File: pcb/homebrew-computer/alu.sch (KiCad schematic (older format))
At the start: 8 parts

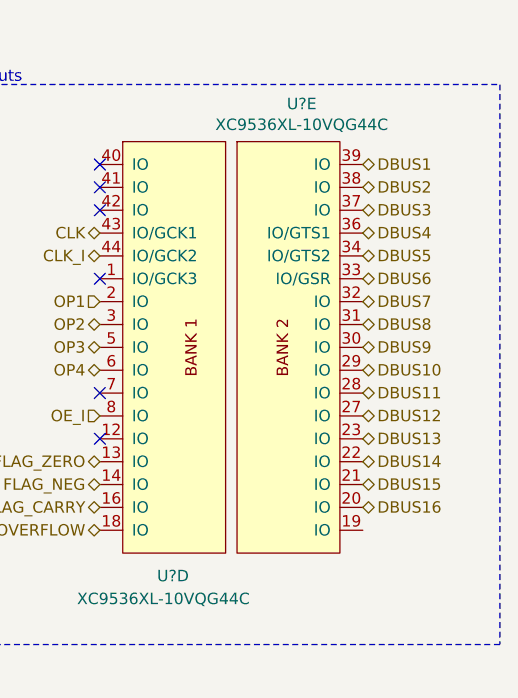
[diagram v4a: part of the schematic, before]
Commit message: Remove the address bus as it would require too big of a connector
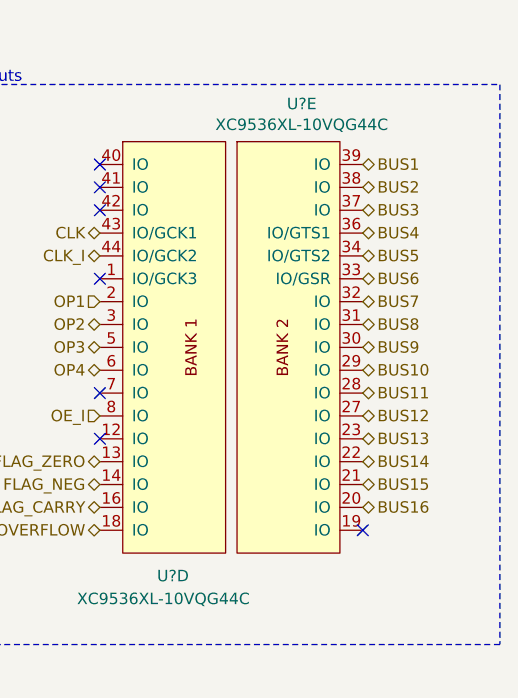
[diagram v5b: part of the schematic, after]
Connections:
- net DBUS1 renamed BUS1
- net DBUS10 renamed BUS10
- net DBUS11 renamed BUS11
- net DBUS12 renamed BUS12
- net DBUS13 renamed BUS13
- net DBUS14 renamed BUS14
- net DBUS15 renamed BUS15
- net DBUS16 renamed BUS16
- net DBUS2 renamed BUS2
- net DBUS3 renamed BUS3
- net DBUS4 renamed BUS4
- net DBUS5 renamed BUS5
- net DBUS6 renamed BUS6
- net DBUS7 renamed BUS7
- net DBUS8 renamed BUS8
- net DBUS9 renamed BUS9
- no-connect marks 6 -> 7
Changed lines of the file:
@@
 $Descr User 8661 5906
 encoding utf-8
-Sheet 4 8
+Sheet 8 7
 Title ""
 Date ""
@@
 Text Notes 1450 3200 0    50   ~ 0
 JTAG
-Text HLabel 6500 1250 2    50   3State ~ 0
-DBUS1
-Text HLabel 6500 1350 2    50   3State ~ 0
-DBUS2
-Text HLabel 6500 1450 2    50   3State ~ 0
-DBUS3
-Text HLabel 6500 1550 2    50   3State ~ 0
-DBUS4
-Text HLabel 6500 1650 2    50   3State ~ 0
-DBUS5
-Text HLabel 6500 1750 2    50   BiDi ~ 0
-DBUS6
-Text HLabel 6500 1850 2    50   BiDi ~ 0
-DBUS7
-Text HLabel 6500 2450 2    50   BiDi ~ 0
-DBUS13
-Text HLabel 6500 2350 2    50   BiDi ~ 0
-DBUS12
-Text HLabel 6500 2250 2    50   BiDi ~ 0
-DBUS11
-Text HLabel 6500 2150 2    50   BiDi ~ 0
-DBUS10
-Text HLabel 6500 2050 2    50   BiDi ~ 0
-DBUS9
-Text HLabel 6500 1950 2    50   BiDi ~ 0
-DBUS8
-Text HLabel 6500 2550 2    50   BiDi ~ 0
-DBUS14
-Text HLabel 6500 2650 2    50   BiDi ~ 0
-DBUS15
-Text HLabel 6500 2750 2    50   BiDi ~ 0
-DBUS16
 Text HLabel 5350 1850 0    50   Input ~ 0
 OP1
@@
 Text HLabel 5350 2350 0    50   Input ~ 0
 OE_I
+Text HLabel 6500 1250 2    50   3State ~ 0
+BUS1
+Text HLabel 6500 1350 2    50   3State ~ 0
+BUS2
+Text HLabel 6500 1450 2    50   3State ~ 0
+BUS3
+Text HLabel 6500 1550 2    50   3State ~ 0
+BUS4
+Text HLabel 6500 1650 2    50   3State ~ 0
+BUS5
+Text HLabel 6500 1750 2    50   3State ~ 0
+BUS6
+Text HLabel 6500 1850 2    50   3State ~ 0
+BUS7
+Text HLabel 6500 1950 2    50   3State ~ 0
+BUS8
+Text HLabel 6500 2050 2    50   3State ~ 0
+BUS9
+Text HLabel 6500 2150 2    50   3State ~ 0
+BUS10
+Text HLabel 6500 2250 2    50   3State ~ 0
+BUS11
+Text HLabel 6500 2350 2    50   3State ~ 0
+BUS12
+Text HLabel 6500 2450 2    50   3State ~ 0
+BUS13
+Text HLabel 6500 2550 2    50   3State ~ 0
+BUS14
+Text HLabel 6500 2650 2    50   3State ~ 0
+BUS15
+Text HLabel 6500 2750 2    50   3State ~ 0
+BUS16
+NoConn ~ 6500 2850
 $EndSCHEMATC

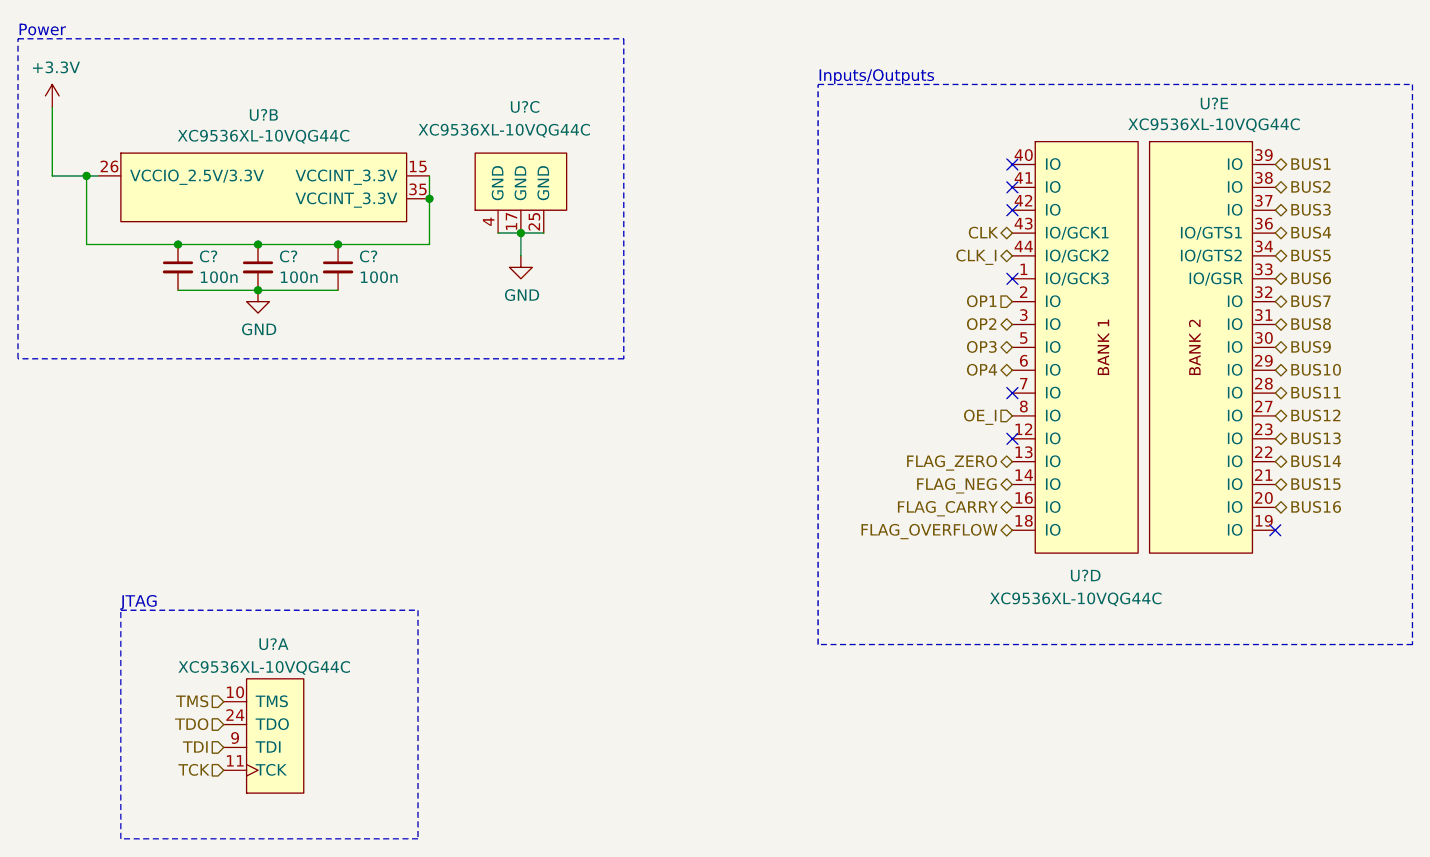
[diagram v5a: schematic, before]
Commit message: Remove unnecessary address bus and unified the IO interface
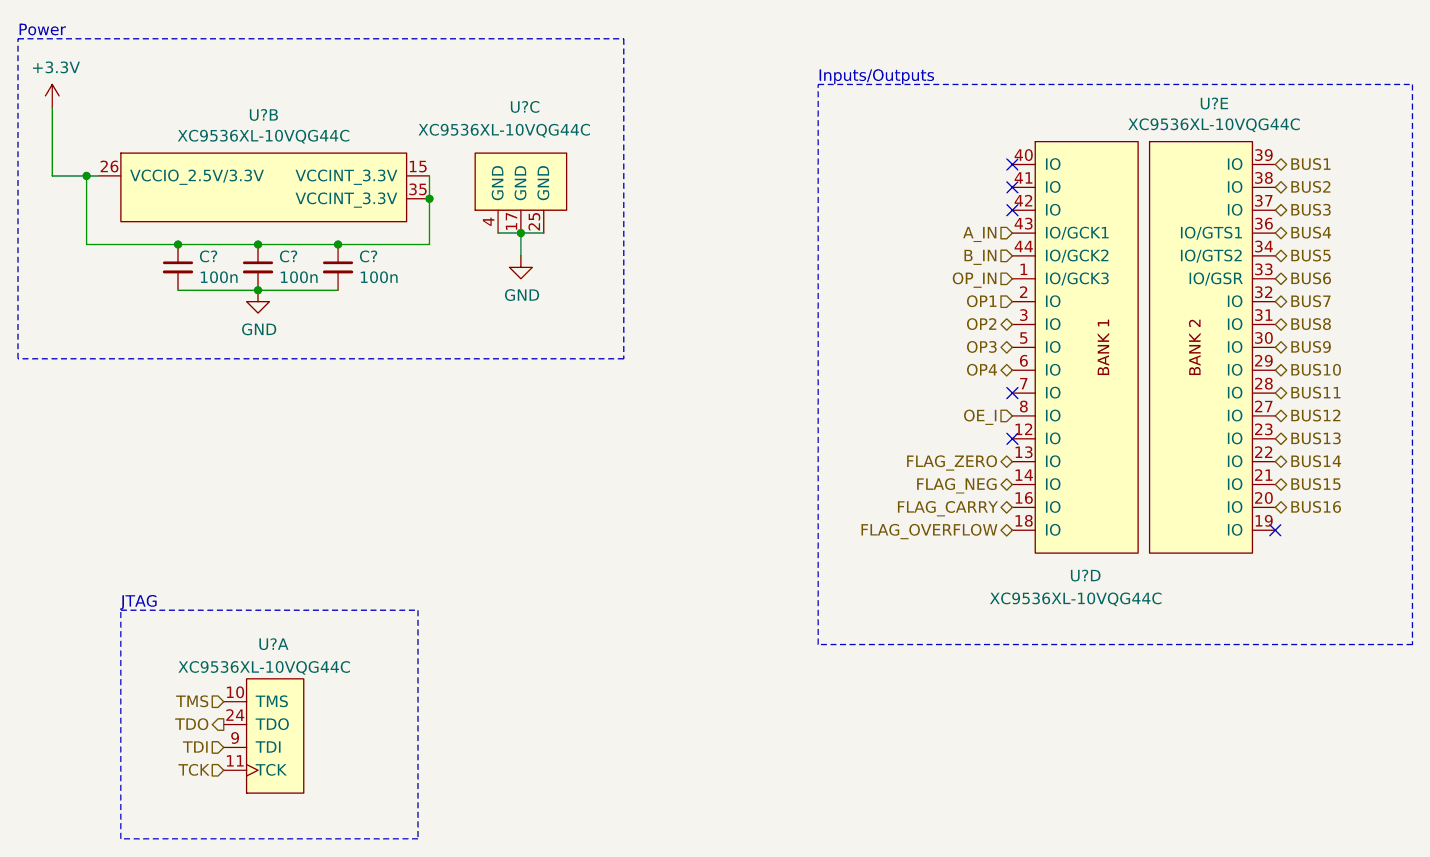
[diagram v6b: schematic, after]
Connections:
- net OP_IN: now reaches U?.1 (IO/GCK3)
- net CLK renamed A_IN
- net CLK_I renamed B_IN
- no-connect marks 7 -> 6
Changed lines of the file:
@@
 $Descr User 8661 5906
 encoding utf-8
-Sheet 8 7
-Title ""
-Date ""
-Rev ""
-Comp ""
+Sheet 3 7
+Title "Arithmetic and Logic Unit"
+Date "2020-10-24"
+Rev "A"
+Comp "cchaine"
 Comment1 ""
 Comment2 ""
@@
 Text HLabel 1900 3600 0    50   Input ~ 0
 TMS
-Text HLabel 1900 3700 0    50   Input ~ 0
+Text HLabel 1900 3700 0    50   Output ~ 0
 TDO
 Text HLabel 1900 3800 0    50   Input ~ 0
@@
 Text HLabel 5350 2150 0    50   3State ~ 0
 OP4
-Text HLabel 5350 1550 0    50   3State ~ 0
-CLK
-Text HLabel 5350 1650 0    50   3State ~ 0
-CLK_I
 Text HLabel 5350 2550 0    50   3State ~ 0
 FLAG_ZERO
@@
 NoConn ~ 5350 1350
 NoConn ~ 5350 1450
-NoConn ~ 5350 1750
 NoConn ~ 5350 2250
 NoConn ~ 5350 2450
@@
 BUS16
 NoConn ~ 6500 2850
+Text HLabel 5350 1550 0    50   Input ~ 0
+A_IN
+Text HLabel 5350 1650 0    50   Input ~ 0
+B_IN
+Text HLabel 5350 1750 0    50   Input ~ 0
+OP_IN
 $EndSCHEMATC

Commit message: Add program counter
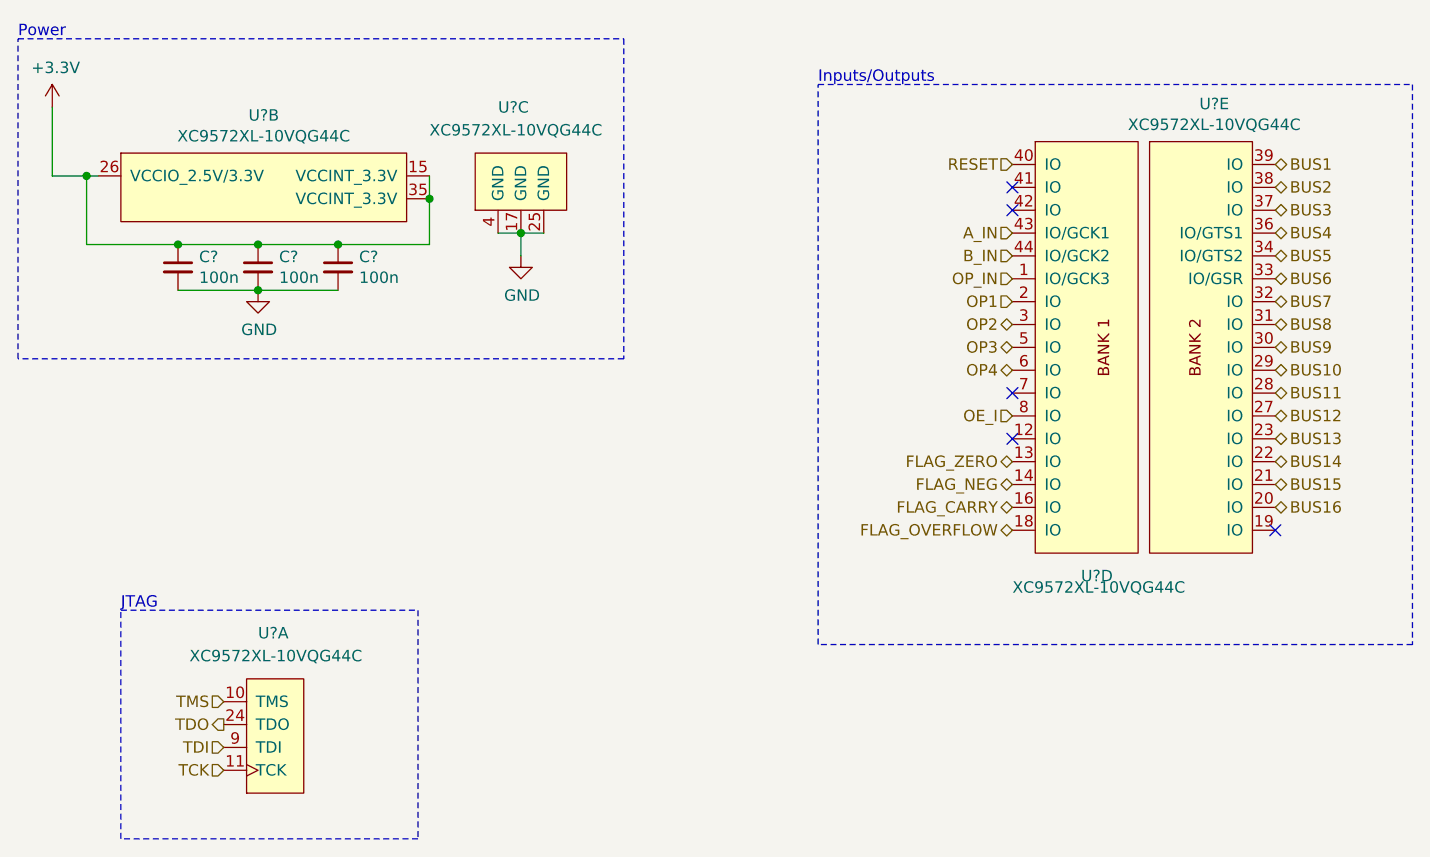
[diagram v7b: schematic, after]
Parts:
- removed U? (x5): XC9536XL-10VQG44C, symbol XC9500XL:XC9536XL-10VQG44C
- added U? (x5): XC9572XL-10VQG44C, symbol XC9500XL:XC9572XL-10VQG44C
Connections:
- net +3V3: now also U?.15 (VCCINT_3.3V), U?.26 (VCCIO_2.5V/3.3V), U?.35 (VCCINT_3.3V)
- net A_IN: now also U?.43 (IO/GCK1)
- net BUS1: now also U?.39 (IO)
- net BUS10: now also U?.29 (IO)
- net BUS11: now also U?.28 (IO)
- net BUS12: now also U?.27 (IO)
- net BUS13: now also U?.23 (IO)
- net BUS14: now also U?.22 (IO)
- net BUS15: now also U?.21 (IO)
- net BUS16: now also U?.20 (IO)
- net BUS2: now also U?.38 (IO)
- net BUS3: now also U?.37 (IO)
- net BUS4: now also U?.36 (IO/GTS1)
- net BUS5: now also U?.34 (IO/GTS2)
- net BUS6: now also U?.33 (IO/GSR)
- net BUS7: now also U?.32 (IO)
- net BUS8: now also U?.31 (IO)
- net BUS9: now also U?.30 (IO)
- net B_IN: now also U?.44 (IO/GCK2)
- net FLAG_CARRY: now also U?.16 (IO)
- net FLAG_NEG: now also U?.14 (IO)
- net FLAG_OVERFLOW: now also U?.18 (IO)
- net FLAG_ZERO: now also U?.13 (IO)
- net GND: now also U?.17 (GND), U?.25 (GND), U?.4 (GND)
- net OE_I: now also U?.8 (IO)
- net OP1: now also U?.2 (IO)
- net OP2: now also U?.3 (IO)
- net OP3: now also U?.5 (IO)
- net OP4: now also U?.6 (IO)
- net OP_IN: now also U?.1 (IO/GCK3)
- net TCK: now also U?.11 (TCK)
- net TDI: now also U?.9 (TDI)
- net TDO: now also U?.24 (TDO)
- net TMS: now also U?.10 (TMS)
- new net RESET: U?.40 (IO)
- no-connect marks 6 -> 5
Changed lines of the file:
@@
 $EndDescr
-$Comp
-L XC9500XL:XC9536XL-10VQG44C U?
-U 1 1 5F8C17B6
-P 2100 4100
-F 0 "U?" H 2150 3350 50  0000 R CNN
-F 1 "XC9536XL-10VQG44C" H 2500 3450 50  0000 R CNN
-F 2 "" H 2100 4100 50  0001 C CNN
-F 3 "" H 2100 4100 50  0001 C CNN
-	1    2100 4100
-	-1   0    0    1
-$EndComp
-$Comp
-L XC9500XL:XC9536XL-10VQG44C U?
-U 2 1 5F8C1C63
-P 2100 1100
-F 0 "U?" H 2075 1165 50  0000 C CNN
-F 1 "XC9536XL-10VQG44C" H 2075 1074 50  0000 C CNN
-F 2 "" H 2100 1100 50  0001 C CNN
-F 3 "" H 2100 1100 50  0001 C CNN
-	2    2100 1100
-	1    0    0    -1
-$EndComp
-$Comp
-L XC9500XL:XC9536XL-10VQG44C U?
-U 4 1 5F8C320A
-P 5700 1050
-F 0 "U?" H 5600 -950 50  0000 L CNN
-F 1 "XC9536XL-10VQG44C" H 5250 -1050 50  0000 L CNN
-F 2 "" H 5700 1050 50  0001 C CNN
-F 3 "" H 5700 1050 50  0001 C CNN
-	4    5700 1050
-	1    0    0    -1
-$EndComp
-$Comp
-L XC9500XL:XC9536XL-10VQG44C U?
-U 5 1 5F8C3B12
-P 6200 1050
-F 0 "U?" H 6233 1115 50  0000 C CNN
-F 1 "XC9536XL-10VQG44C" H 6233 1024 50  0000 C CNN
-F 2 "" H 6200 1050 50  0001 C CNN
-F 3 "" H 6200 1050 50  0001 C CNN
-	5    6200 1050
-	1    0    0    -1
-$EndComp
 $Comp
 L power:+3.3V #PWR0109
@@
 	2050 1600 2400 1600
 Wire Wire Line
-	2800 1300 2800 1400
-Wire Wire Line
 	2800 1600 2400 1600
-Connection ~ 2800 1400
-Wire Wire Line
-	2800 1400 2800 1600
 Connection ~ 2400 1600
 Wire Wire Line
@@
 Wire Wire Line
 	3100 1550 3200 1550
-$Comp
-L XC9500XL:XC9536XL-10VQG44C U?
-U 3 1 5F8C2422
-P 2850 1350
-F 0 "U?" V 3200 1050 50  0000 R CNN
-F 1 "XC9536XL-10VQG44C" V 3100 1450 50  0000 R CNN
-F 2 "" H 2850 1350 50  0001 C CNN
-F 3 "" H 2850 1350 50  0001 C CNN
-	3    2850 1350
-	0    -1   -1   0
-$EndComp
 $Comp
 L power:GND #PWR0111
@@
 Text HLabel 5350 2850 0    50   3State ~ 0
 FLAG_OVERFLOW
-NoConn ~ 5350 1250
 NoConn ~ 5350 1350
 NoConn ~ 5350 1450
@@
 Text HLabel 5350 1750 0    50   Input ~ 0
 OP_IN
+$Comp
+L XC9500XL:XC9572XL-10VQG44C U?
+U 1 1 5F975DA0
+P 2100 4100
+F 0 "U?" H 2150 3300 50  0000 R CNN
+F 1 "XC9572XL-10VQG44C" H 2450 3400 50  0000 R CNN
+F 2 "" H 2100 4100 50  0001 C CNN
+F 3 "" H 2100 4100 50  0001 C CNN
+	1    2100 4100
+	-1   0    0    1
+$EndComp
+$Comp
+L XC9500XL:XC9572XL-10VQG44C U?
+U 2 1 5F97A638
+P 2100 1100
+F 0 "U?" H 2075 1165 50  0000 C CNN
+F 1 "XC9572XL-10VQG44C" H 2075 1074 50  0000 C CNN
+F 2 "" H 2100 1100 50  0001 C CNN
+F 3 "" H 2100 1100 50  0001 C CNN
+	2    2100 1100
+	1    0    0    -1
+$EndComp
+Wire Wire Line
+	2800 1400 2800 1600
+Wire Wire Line
+	2800 1400 2800 1300
+Connection ~ 2800 1400
+$Comp
+L XC9500XL:XC9572XL-10VQG44C U?
+U 3 1 5F97D3D1
+P 2850 1350
+F 0 "U?" V 3200 1100 50  0000 R CNN
+F 1 "XC9572XL-10VQG44C" V 3100 1400 50  0000 R CNN
+F 2 "" H 2850 1350 50  0001 C CNN
+F 3 "" H 2850 1350 50  0001 C CNN
+	3    2850 1350
+	0    -1   -1   0
+$EndComp
+$Comp
+L XC9500XL:XC9572XL-10VQG44C U?
+U 4 1 5F982A18
+P 5700 1050
+F 0 "U?" H 5650 -950 50  0000 L CNN
+F 1 "XC9572XL-10VQG44C" H 5350 -1000 50  0000 L CNN
+F 2 "" H 5700 1050 50  0001 C CNN
+F 3 "" H 5700 1050 50  0001 C CNN
+	4    5700 1050
+	1    0    0    -1
+$EndComp
+$Comp
+L XC9500XL:XC9572XL-10VQG44C U?
+U 5 1 5F987E07
+P 6200 1050
+F 0 "U?" H 6233 1115 50  0000 C CNN
+F 1 "XC9572XL-10VQG44C" H 6233 1024 50  0000 C CNN
+F 2 "" H 6200 1050 50  0001 C CNN
+F 3 "" H 6200 1050 50  0001 C CNN
+	5    6200 1050
+	1    0    0    -1
+$EndComp
+Text HLabel 5350 1250 0    50   Input ~ 0
+RESET
 $EndSCHEMATC

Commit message: Change the control logic CPLD for a bigger one
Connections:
- net BUS10: now also U?.27 (IO); no longer U?.29 (IO)
- net BUS11: now also U?.23 (IO); no longer U?.28 (IO)
- net BUS12: now also U?.22 (IO); no longer U?.27 (IO)
- net BUS13: now also U?.21 (IO); no longer U?.23 (IO)
- net BUS14: now also U?.20 (IO); no longer U?.22 (IO)
- net BUS15: now also U?.19 (IO); no longer U?.21 (IO)
- net BUS16: now also U?.40 (IO); no longer U?.20 (IO)
- net BUS4: now also U?.34 (IO/GTS2); no longer U?.36 (IO/GTS1)
- net BUS5: now also U?.32 (IO); no longer U?.34 (IO/GTS2)
- net BUS6: now also U?.31 (IO); no longer U?.33 (IO/GSR)
- net BUS7: now also U?.30 (IO); no longer U?.32 (IO)
- net BUS8: now also U?.29 (IO); no longer U?.31 (IO)
- net BUS9: now also U?.28 (IO); no longer U?.30 (IO)
- net RESET: now also U?.33 (IO/GSR); no longer U?.40 (IO)
- net OE_I: no longer names the net of U?.8 (IO)
- new net ALU_OUT_I: U?.36 (IO/GTS1)
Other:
- note added: "ALU_OUT_I is wired to the GTS1 to\nprovide minimum skew to most macrocells"
- note added: "RESET is wired to GSR to\nprovide minimum skew to most macrocells"
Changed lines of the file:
@@
 Text Notes 4500 900  0    50   ~ 0
 Inputs/Outputs
-Text HLabel 5350 2350 0    50   Input ~ 0
-OE_I
+Text HLabel 6500 1550 2    50   Input ~ 0
+ALU_OUT_I
 Text HLabel 6500 1250 2    50   3State ~ 0
 BUS1
@@
 Text HLabel 6500 1450 2    50   3State ~ 0
 BUS3
-Text HLabel 6500 1550 2    50   3State ~ 0
+Text HLabel 6500 1650 2    50   3State ~ 0
 BUS4
-Text HLabel 6500 1650 2    50   3State ~ 0
+Text HLabel 6500 1850 2    50   3State ~ 0
 BUS5
-Text HLabel 6500 1750 2    50   3State ~ 0
+Text HLabel 6500 1950 2    50   3State ~ 0
 BUS6
-Text HLabel 6500 1850 2    50   3State ~ 0
+Text HLabel 6500 2050 2    50   3State ~ 0
 BUS7
-Text HLabel 6500 1950 2    50   3State ~ 0
+Text HLabel 6500 2150 2    50   3State ~ 0
 BUS8
-Text HLabel 6500 2050 2    50   3State ~ 0
+Text HLabel 6500 2250 2    50   3State ~ 0
 BUS9
-Text HLabel 6500 2150 2    50   3State ~ 0
+Text HLabel 6500 2350 2    50   3State ~ 0
 BUS10
-Text HLabel 6500 2250 2    50   3State ~ 0
+Text HLabel 6500 2450 2    50   3State ~ 0
 BUS11
-Text HLabel 6500 2350 2    50   3State ~ 0
+Text HLabel 6500 2550 2    50   3State ~ 0
 BUS12
-Text HLabel 6500 2450 2    50   3State ~ 0
+Text HLabel 6500 2650 2    50   3State ~ 0
 BUS13
-Text HLabel 6500 2550 2    50   3State ~ 0
+Text HLabel 6500 2750 2    50   3State ~ 0
 BUS14
-Text HLabel 6500 2650 2    50   3State ~ 0
+Text HLabel 6500 2850 2    50   3State ~ 0
 BUS15
-Text HLabel 6500 2750 2    50   3State ~ 0
+Text HLabel 5350 1250 0    50   3State ~ 0
 BUS16
-NoConn ~ 6500 2850
 Text HLabel 5350 1550 0    50   Input ~ 0
 A_IN
@@
 	1    0    0    -1
 $EndComp
-Text HLabel 5350 1250 0    50   Input ~ 0
+Text HLabel 6500 1750 2    50   Input ~ 0
 RESET
+NoConn ~ 5350 2350
+Text Notes 4500 3550 0    50   Italic 0
+ALU_OUT_I is wired to the GTS1 to\nprovide minimum skew to most macrocells
+Text Notes 4500 3800 0    50   Italic 0
+RESET is wired to GSR to\nprovide minimum skew to most macrocells
 $EndSCHEMATC
